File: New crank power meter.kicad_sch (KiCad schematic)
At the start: 14 parts, among them U1 ESP32-S3-MINI-1, U2 MCP1825S

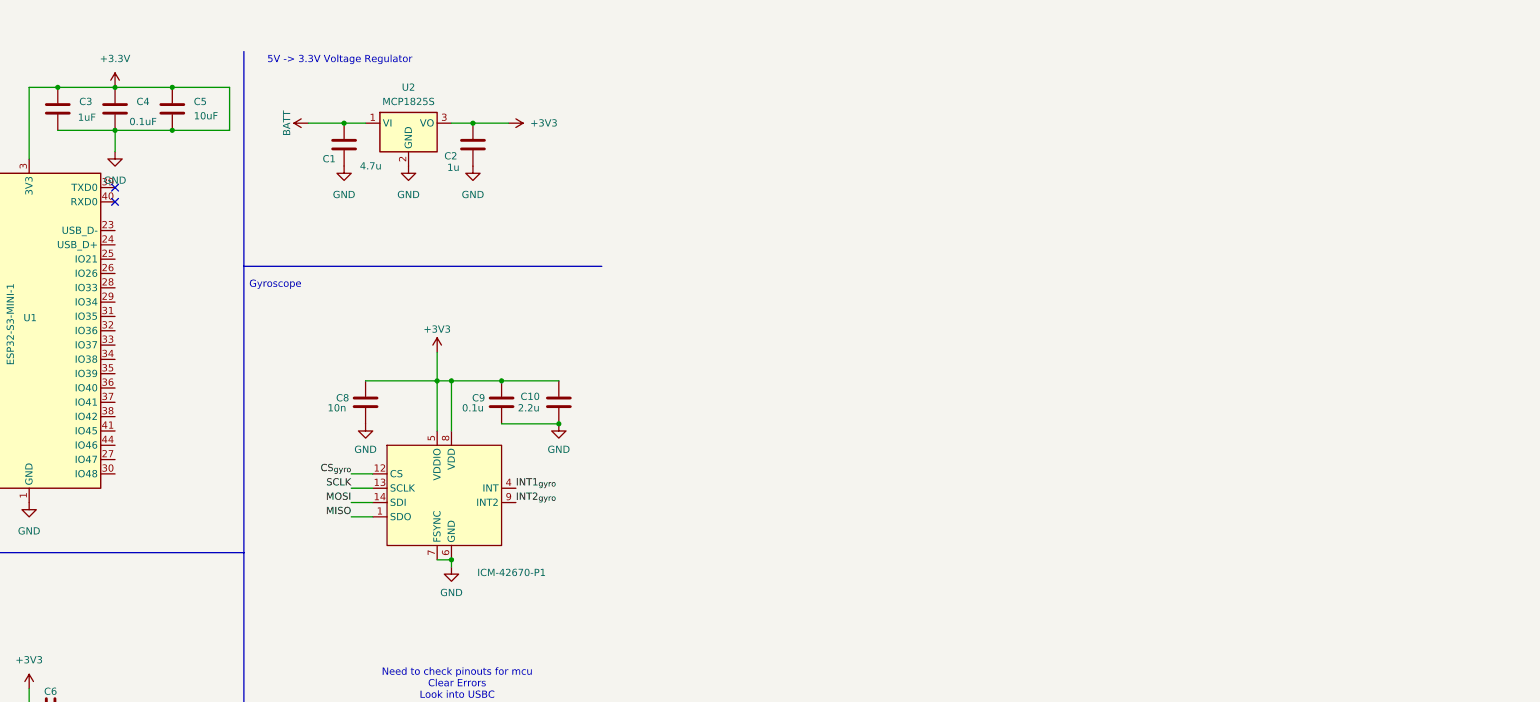
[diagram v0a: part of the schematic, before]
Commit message: added status leds, strain gauge header
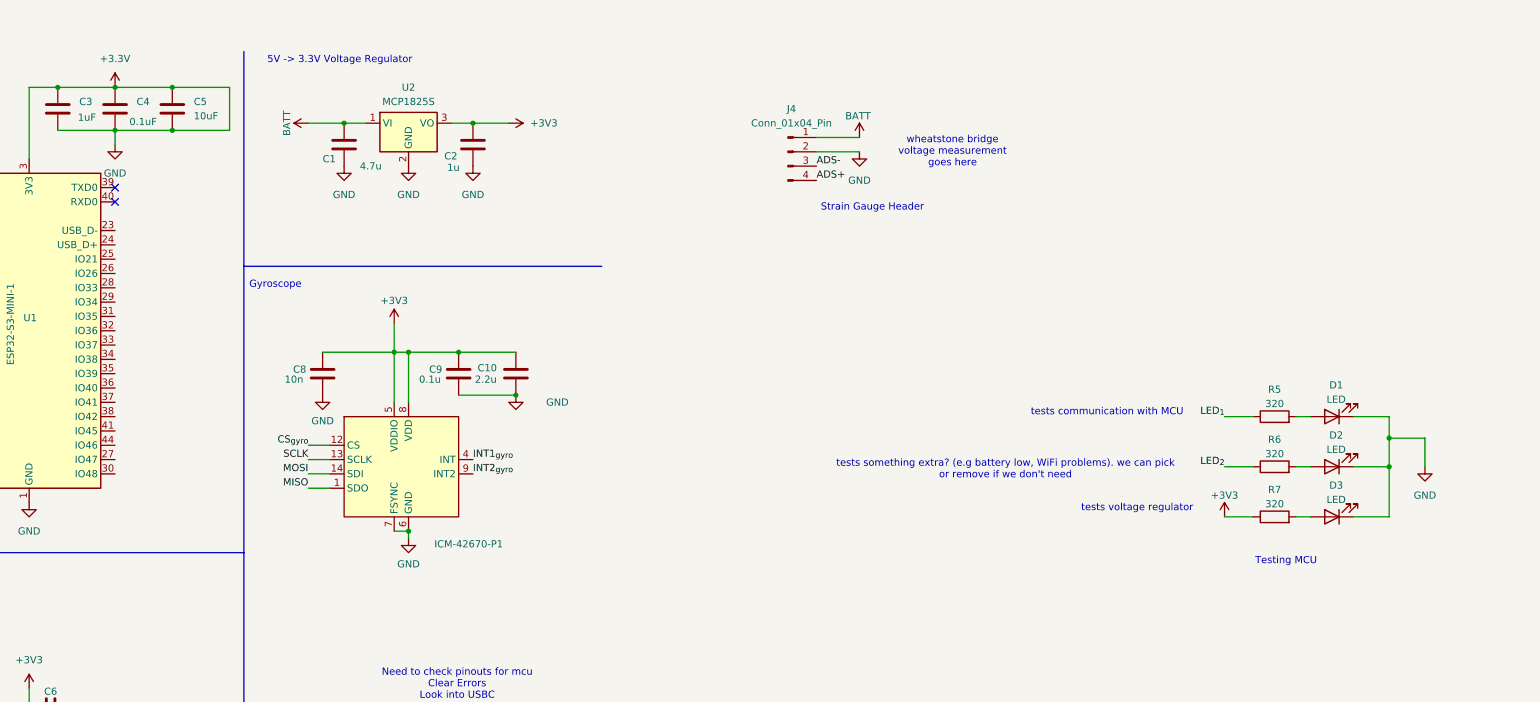
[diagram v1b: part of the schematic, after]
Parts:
- added D1, D2, D3: LED, LED_SMD:LED_0402_1005Metric, symbol Device:LED
- added J4: Conn_01x04_Pin, Connector_JST:JST_EH_S4B-EH_1x04_P2.50mm_Horizontal, symbol Connector:Conn_01x04_Pin
- added R5, R6, R7: 320, Resistor_SMD:R_0402_1005Metric, symbol Device:R
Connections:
- net +3.3V: now also D1.1 (K), D2.1 (K), D3.1 (K), J4.2 (Pin_2)
- net +3V3: now also R7.1
- net ADS+: now also J4.4 (Pin_4)
- net ADS-: now also J4.3 (Pin_3)
- net BATT: now also J4.1 (Pin_1)
- new net: D1.2 (A), R5.2
- new net: D3.2 (A), R7.2
- new net: D2.2 (A), R6.2
- new net LED_{1}: R5.1
- new net LED_{2}: R6.1
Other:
- note added: "Strain Gauge Header"
- note added: "Testing MCU"
- note added: "tests communication with MCU"
- note added: "tests something extra? (e.g battery low, WiFi problems). we can pick or remove if we don't need"
- note added: "tests voltage regulator"
- note added: "wheatstone bridge voltage measurement goes here"
- moved on the sheet: C10, C8, C9, ICM-42670-P1

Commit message: notes
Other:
- note added: "Can look into an external analog digital converter, apparently the one in the mcu isnt very precise for the strain gauge signals we are reading"
- note added: "Figure out bluetooth low energy, and battery"
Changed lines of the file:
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@@
+		)
+	)
+	(text "Figure out bluetooth low energy, and battery"
+		(exclude_from_sim no)
+		(at 44.196 191.516 0)
+		(effects
+			(font
+				(size 1.27 1.27)
+			)
+		)
+	)
+	(text "Can look into an external analog digital converter, apparently the one in the mcu isnt very precise for the strain gauge signals we are reading"
+		(exclude_from_sim no)
+		(at 93.726 188.214 0)
+		(effects
+			(font
+				(size 1.27 1.27)
+			)
 		)
 	)

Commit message: added Hx711
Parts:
- added U3: HX711, Package_SO:SOP-16_3.9x9.9mm_P1.27mm, symbol Analog_ADC:HX711
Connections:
- net +3.3V: now also U3.14 (XI), U3.5 (AGND)
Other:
- note added: "ADC and load cell amplifier in one"
- note added: "Noah: battery should be pretty simple, connect to voltage reg according to datasheet bluetooth low energy is built into the MCU, we just have to code it with the right library"
- note added: "Status LED's for MCU"
- note added: "check the OLD schematic in Github, I had all the connections from the guy I copied for HX711"
- note removed: "Testing MCU"
- moved on the sheet: D1, D2, D3, R5, R6, R7

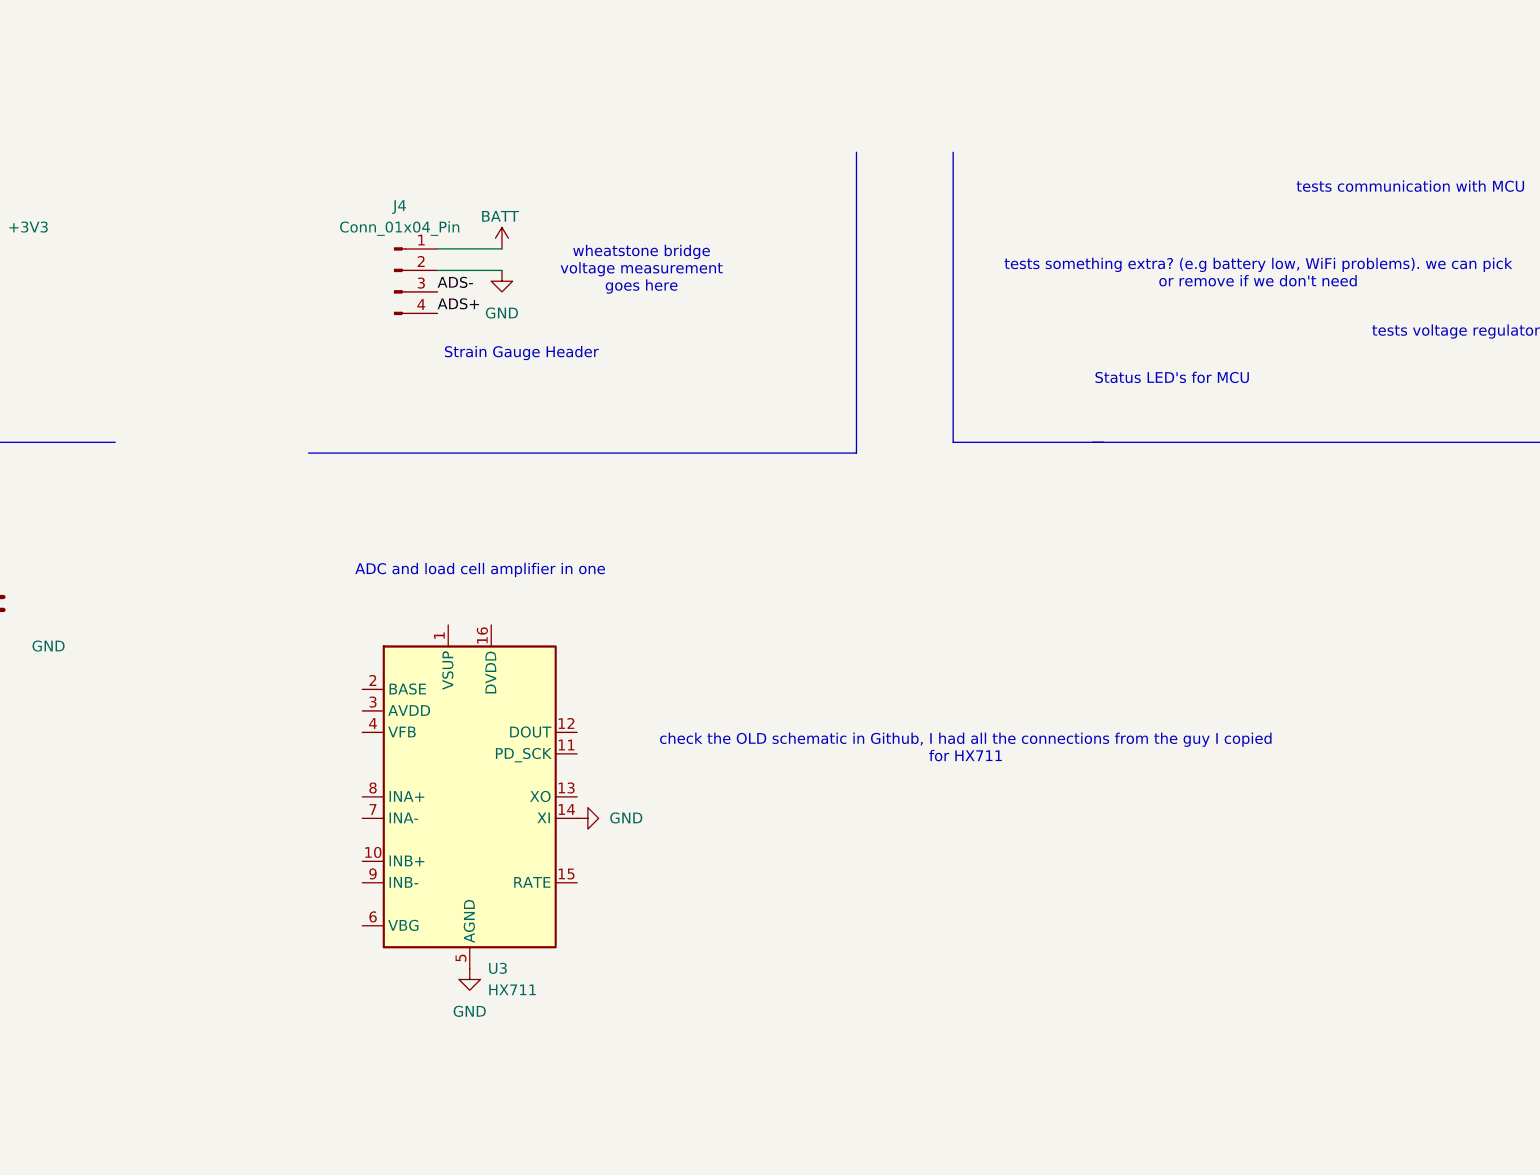
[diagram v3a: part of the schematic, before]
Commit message: HX711 more pins added
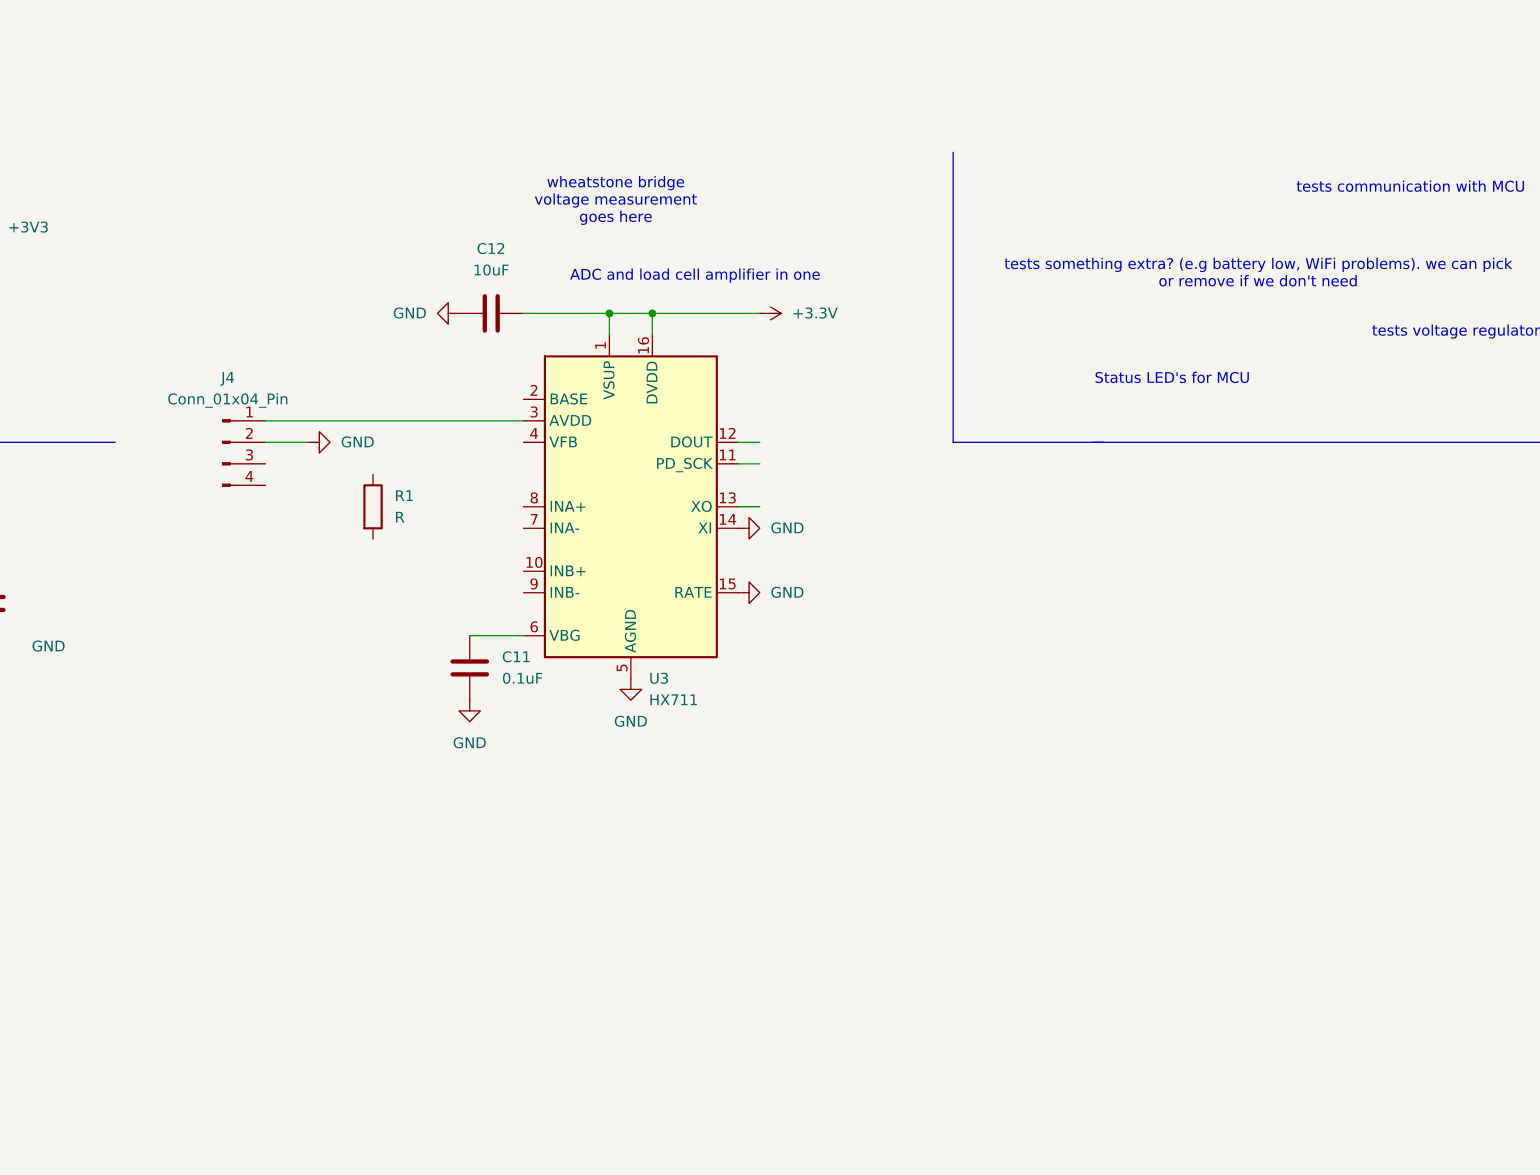
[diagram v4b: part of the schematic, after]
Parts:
- added C11: 0.1uF, symbol Device:C
- added C12: 10uF, symbol Device:C
- added R1: R, symbol Device:R
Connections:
- net +3.3V: now also U3.1 (VSUP), U3.15 (RATE), U3.16 (DVDD), C11.2, C12.1, C12.2
- net ADS+: no longer J4.4 (Pin_4)
- net ADS-: no longer J4.3 (Pin_3)
- net BATT: no longer J4.1 (Pin_1)
- net at U3.3 (AVDD): now also J4.1 (Pin_1)
- net at U3.6 (VBG): now also C11.1
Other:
- note removed: "Strain Gauge Header"
- note removed: "check the OLD schematic in Github, I had all the connections from the guy I copied for HX711"
- moved on the sheet: J4, U3

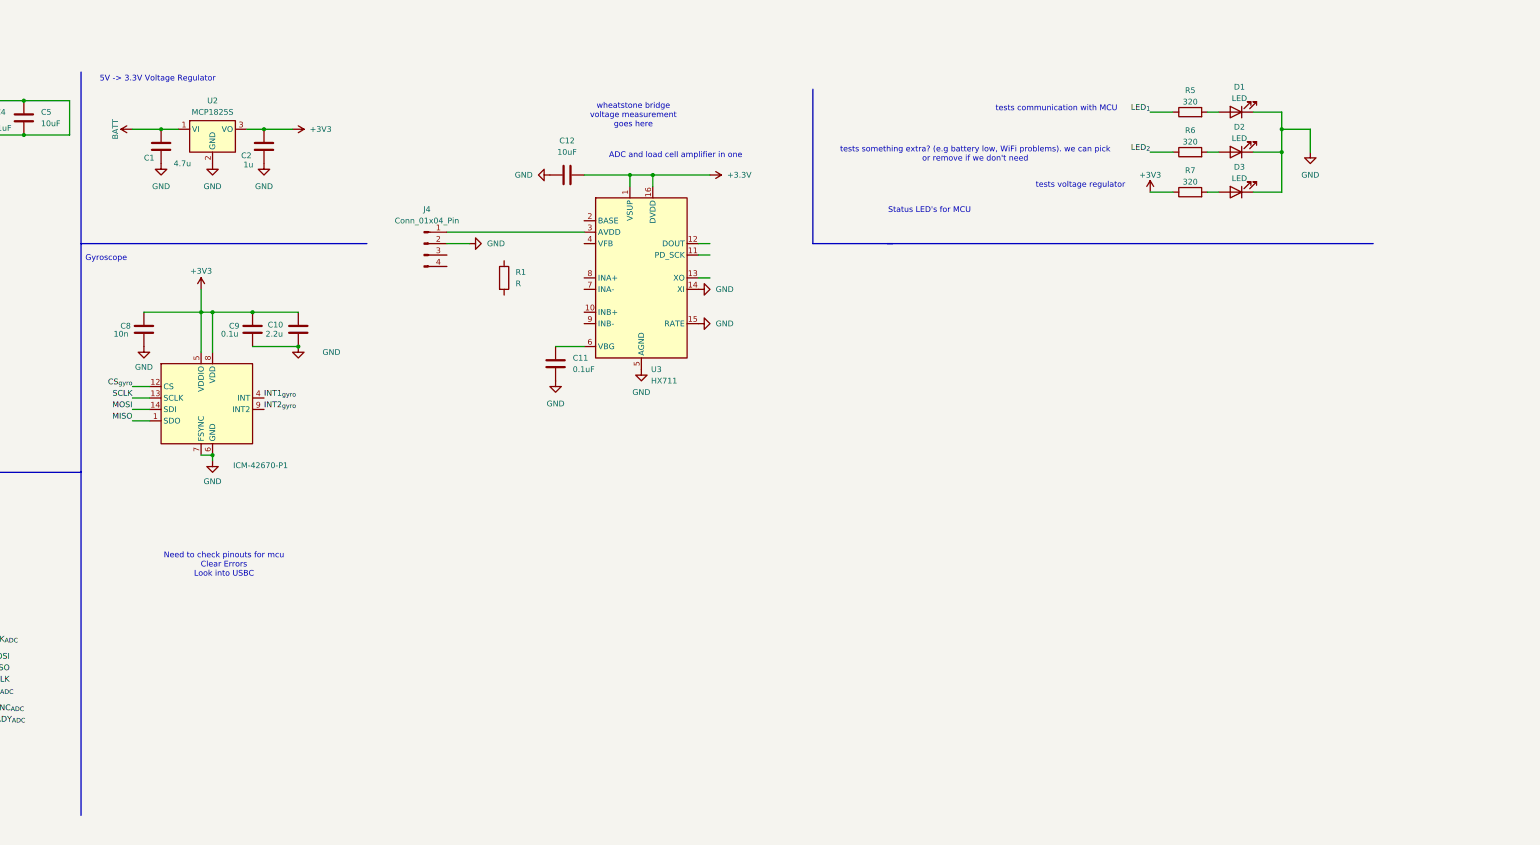
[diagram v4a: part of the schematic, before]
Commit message: more pins on hx711
the datasheet has an example schematic, i've been following that
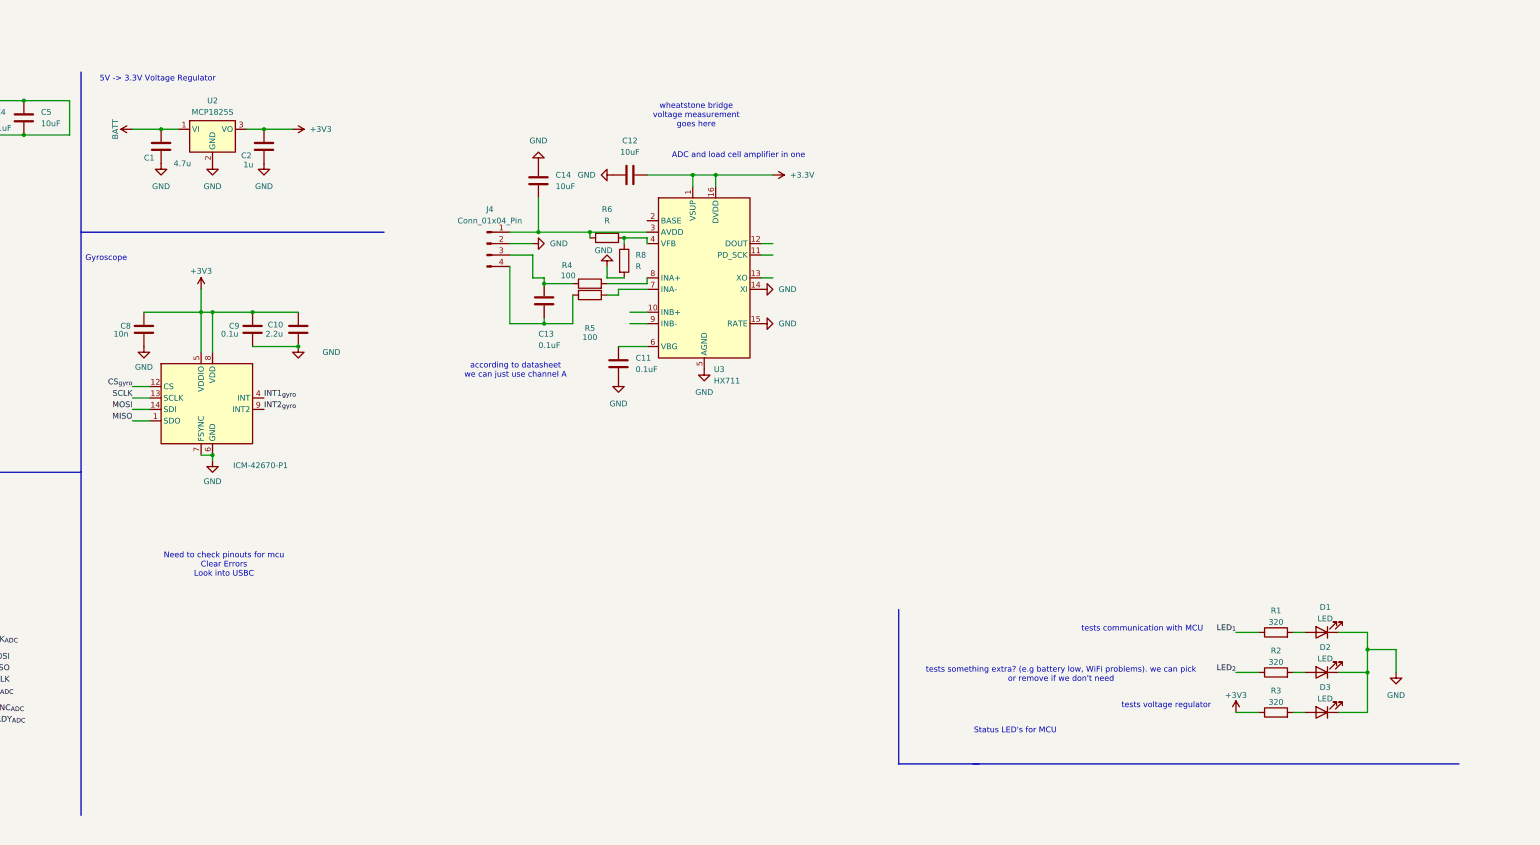
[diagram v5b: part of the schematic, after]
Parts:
- added C13: 0.1uF, symbol Device:C
- added C14: 10uF, symbol Device:C
- added R5: 100, symbol Device:R
- added R6, R8: R, symbol Device:R
- R4: renamed from R1; value R -> 100
- renumbered R5 to R1, R6 to R2, R7 to R3
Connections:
- net +3.3V: now also C14.1, R8.2
- net at J4.1 (Pin_1), U3.3 (AVDD): now also C14.2, R6.1
- net at J4.3 (Pin_3): now also R4.1, C13.1
- net at J4.4 (Pin_4): now also C13.2, R5.2
- net at R4.2: now also U3.8 (INA+)
- net at U3.4 (VFB): now also R6.2, R8.1
- net at U3.7 (INA-): now also R5.1
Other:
- note added: "according to datasheet we can just use channel A"
- moved on the sheet: C11, C12, D1, D2, D3, J4, R1, R2, R3, R4, U3

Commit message: adding more pins, cleaning up
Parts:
- removed ADS131M1: ~, 0_stuff:ads, symbol 0_pwrmtr:ADS131M03
- removed C6: 1uF, Capacitor_SMD:C_0402_1005Metric, symbol Device:C
- removed C7: 220n, Capacitor_SMD:C_0402_1005Metric, symbol Device:C
- removed D2: LED, LED_SMD:LED_0402_1005Metric, symbol Device:LED
- removed R2: 320, Resistor_SMD:R_0402_1005Metric, symbol Device:R
- added Q1: PNP, symbol Simulation_SPICE:PNP
- R6: value R -> 20k
- R8: value R -> 8.2k
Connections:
- net +3.3V: now also Q1.3 (E)
- net at C14.2, J4.1 (Pin_1), R6.1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: now also Q1.1 (C)
- net at U3.2 (BASE): now also Q1.2 (B)
- net LED_{1} renamed LED
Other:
- note added: "CS Gyro"
- note added: "HX711 DOUT"
- note added: "HX711 PDSCK"
- note added: "INT Gyro"
- note added: "INT_{2} Gyro"
- note added: "LED"
- note added: "MCU GPIO"
- note added: "MISO Gyro"
- note added: "MOSI Gyro"
- note added: "strain gauge (w/ wheatstone measurement)"
- note removed: "Strain Gauge Amplifier"
- note removed: "tests something extra? (e.g battery low, WiFi problems). we can pick or remove if we don't need"
- note removed: "wheatstone bridge voltage measurement goes here"
- moved on the sheet: C10, C11, C12, C13, C14, C8, C9, D1, D3, ICM-42670-P1, J4, R1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
